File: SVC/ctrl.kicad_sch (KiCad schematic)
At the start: 7 parts, among them U15 AD8620

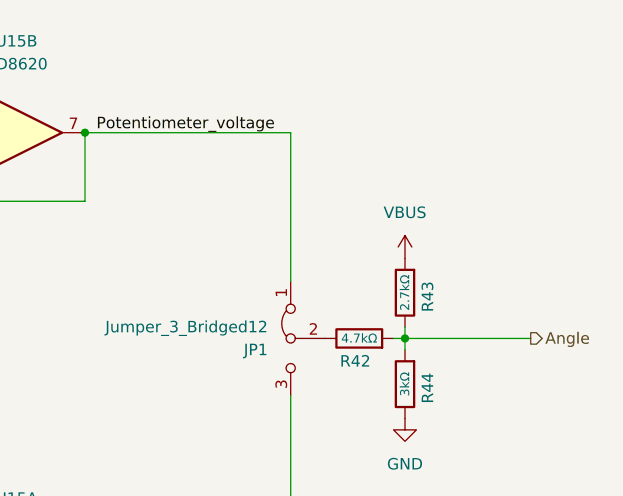
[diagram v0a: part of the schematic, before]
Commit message: did some layout work, minor schematic changes to help with layout
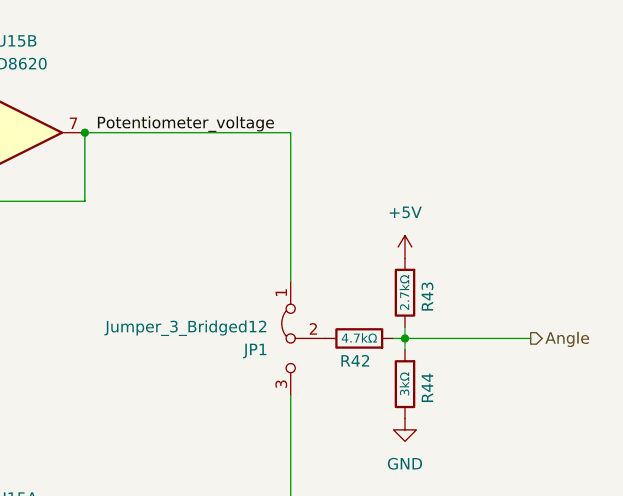
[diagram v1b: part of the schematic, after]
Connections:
- net VBUS is gone; now on net +5V: R43.2
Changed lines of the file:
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@@
     (effects (font (size 1.27 1.27)) (justify left))
-  )
-  (symbol (lib_id "power:VBUS") (at 248.92 77.47 0) (unit 1)
-    (in_bom yes) (on_board yes) (dnp no) (fields_autoplaced)
-    (property "Reference" "#PWR0106" (at 248.92 81.28 0)
-      (effects (font (size 1.27 1.27)) hide)
-    )
-    (property "Value" "VBUS" (at 248.92 72.39 0)
-      (effects (font (size 1.27 1.27)))
-    )
-    (property "Footprint" "" (at 248.92 77.47 0)
-      (effects (font (size 1.27 1.27)) hide)
-    )
-    (property "Datasheet" "" (at 248.92 77.47 0)
-      (effects (font (size 1.27 1.27)) hide)
-    )
-    (pin "1")
-    (instances
-      (project "SVC"
-        (path "/ea5b99b2-c73f-42ef-b805-75088c888f14/27ff332c-3fa5-4494-9372-5966c25dd818"
-          (reference "#PWR0106") (unit 1)
-        )
-      )
-    )
   )
   (symbol (lib_id "power:GND") (at 127 180.34 0) (unit 1)
@@
         )
       )
+    )
+  )
+  (symbol (lib_id "power:+5V") (at 248.92 77.47 0) (unit 1)
+    (in_bom yes) (on_board yes) (dnp no) (fields_autoplaced)
+    (property "Reference" "#PWR0106" (at 248.92 81.28 0)
+      (effects (font (size 1.27 1.27)) hide)
+    )
+    (property "Value" "+5V" (at 248.92 72.39 0)
+      (effects (font (size 1.27 1.27)))
+    )
+    (property "Footprint" "" (at 248.92 77.47 0)
+      (effects (font (size 1.27 1.27)) hide)
+    )
+    (property "Datasheet" "" (at 248.92 77.47 0)
+      (effects (font (size 1.27 1.27)) hide)
+    )
+    (pin "1")
+    (instances
+      (project "SVC"
+        (path "/ea5b99b2-c73f-42ef-b805-75088c888f14/27ff332c-3fa5-4494-9372-5966c25dd818"
+          (reference "#PWR0106") (unit 1)
+        )
+      )
